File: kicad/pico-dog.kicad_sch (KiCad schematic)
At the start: 8 parts

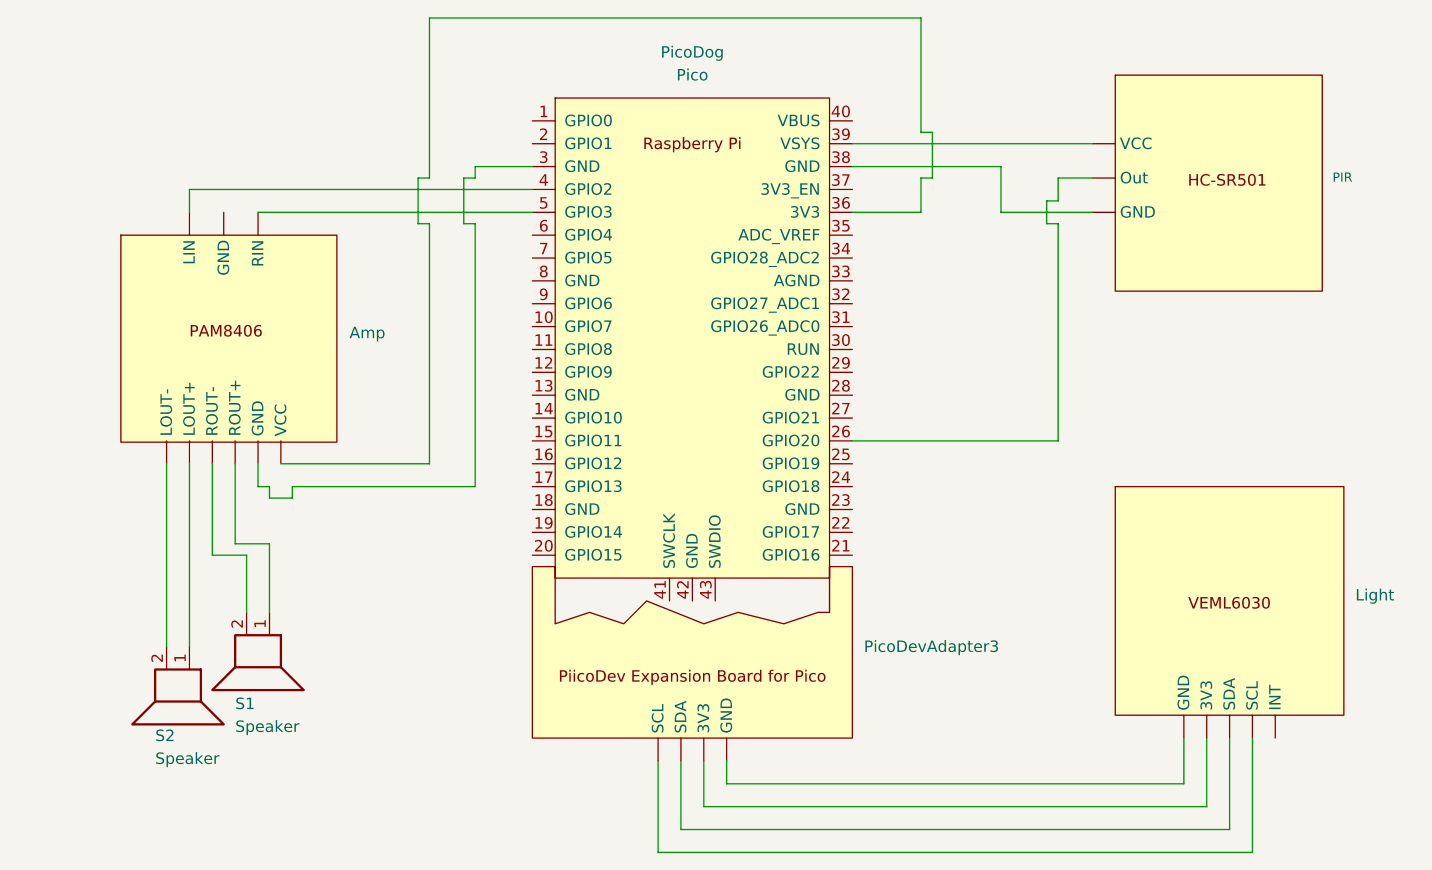
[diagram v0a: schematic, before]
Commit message: update schematic
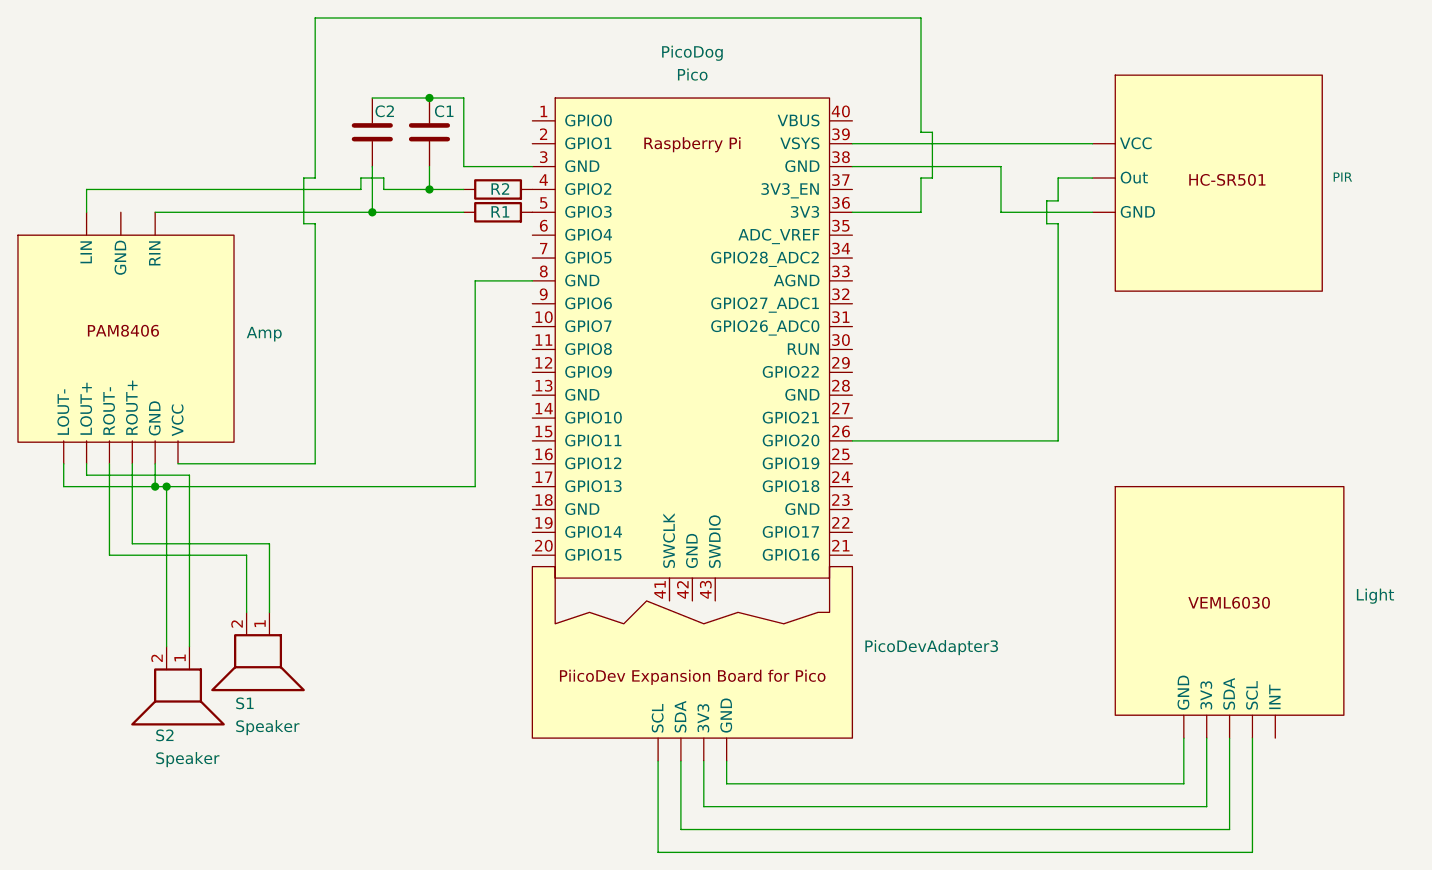
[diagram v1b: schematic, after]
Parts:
- added C1, C2: C, symbol Device:C
- added R1, R2: R, symbol Device:R
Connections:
- net at Amp. (VCC): now also S1.2
- net at Amp. (VCC), S2.2: now also PicoDog.8 (GND)
- net at PicoDog.3 (GND): now also C1.2, C2.2; no longer Amp. (VCC)
- net at PicoDog.4 (GPIO2): now also R2.2; no longer Amp. (VCC)
- net at PicoDog.5 (GPIO3): now also R1.2; no longer Amp. (VCC)
- net at Light. (SDA): now also PicoDevAdapter3. (SDA)
- new net: Amp. (VCC), C1.1, R2.1
- new net: Amp. (VCC), C2.1, R1.1
- new net: Light. (SDA), PicoDevAdapter3. (SDA) (x3)
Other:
- moved on the sheet: Amp

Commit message: Update port to 27 and pictures
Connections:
- net at PIR. (VCC): now also PicoDog.39 (VSYS); no longer PicoDog.26 (GPIO20)
- net at Amp. (VCC): now also S1.2
- net at Light. (SDA): now also PicoDevAdapter3. (SDA)
- net at PicoDog.27 (GPIO21): now also PIR. (VCC)
- new net: Light. (SDA), PicoDevAdapter3. (SDA) (x3)
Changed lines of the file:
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@@
-	(wire
-		(pts
-			(xy 156.21 87.63) (xy 179.07 87.63)
-		)
-		(stroke
-			(width 0)
-			(type default)
-		)
-	)
 	(wire
 		(pts
@@
 	(wire
 		(pts
+			(xy 156.21 85.09) (xy 179.07 85.09)
+		)
+		(stroke
+			(width 0)
+			(type default)
+		)
+	)
+	(wire
+		(pts
 			(xy 71.12 90.17) (xy 71.12 91.44)
 		)
@@
 	(wire
 		(pts
-			(xy 179.07 63.5) (xy 179.07 87.63)
-		)
-		(stroke
+			(xy 179.07 63.5) (xy 179.07 85.09)
+		)
+		(stroke

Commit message: Update kickad
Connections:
- net at Amp. (VCC): now also S1.2
- net at Light. (SDA): now also PicoDevAdapter3. (SDA)
- new net: Light. (SDA), PicoDevAdapter3. (SDA) (x3)

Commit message: fix wiring error
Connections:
- net at PIR. (GND): now also PicoDog.39 (VSYS); no longer PicoDog.27 (GPIO21)
- net at Amp. (VCC): now also S1.2
- net at Light. (INT): now also PicoDevAdapter3. (GND)
- net at PicoDog.28 (GND): now also PicoDog.27 (GPIO21)
- net at PicoDog.32 (GPIO27_ADC1): now also PIR. (GND)
- new net: Light. (INT), PicoDevAdapter3. (GND) (x3)
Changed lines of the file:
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@@
 (kicad_sch
-	(version 20231120)
+	(version 20250114)
 	(generator "eeschema")
-	(generator_version "8.0")
+	(generator_version "9.0")
 	(paper "A4")
 	(title_block
@@
 	(wire
 		(pts
+			(xy 179.07 63.5) (xy 179.07 72.39)
+		)
+		(stroke
+			(width 0)
+			(type default)
+		)
+	)
+	(wire
+		(pts
 			(xy 91.44 99.06) (xy 91.44 106.68)
 		)
@@
 	(wire
 		(pts
+			(xy 156.21 82.55) (xy 156.21 85.09)
+		)
+		(stroke
+			(width 0)
+			(type default)
+		)
+	)
+	(wire
+		(pts
 			(xy 114.3 69.85) (xy 120.65 69.85)
 		)
@@
 	(wire
 		(pts
+			(xy 179.07 72.39) (xy 156.21 72.39)
+		)
+		(stroke
+			(width 0)
+			(type default)
+		)
+	)
+	(wire
+		(pts
 			(xy 142.24 125.73) (xy 193.04 125.73)
 		)
@@
 	(wire
 		(pts
-			(xy 156.21 85.09) (xy 179.07 85.09)
-		)
-		(stroke
-			(width 0)
-			(type default)
-		)
-	)
-	(wire
-		(pts
 			(xy 71.12 90.17) (xy 71.12 91.44)
 		)
@@
 		(pts
 			(xy 109.22 57.15) (xy 109.22 59.69)
-		)
-		(stroke
-			(width 0)
-			(type default)
-		)
-	)
-	(wire
-		(pts
-			(xy 179.07 63.5) (xy 179.07 85.09)
 		)
 		(stroke
@@
 		)
 	)
+	(embedded_fonts no)
 )
